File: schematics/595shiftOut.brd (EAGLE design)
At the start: 160 x 100 mm, 7 parts, among them IC1 74HC595N, IC2 74HC595N, U1 TINY45-20-DIP

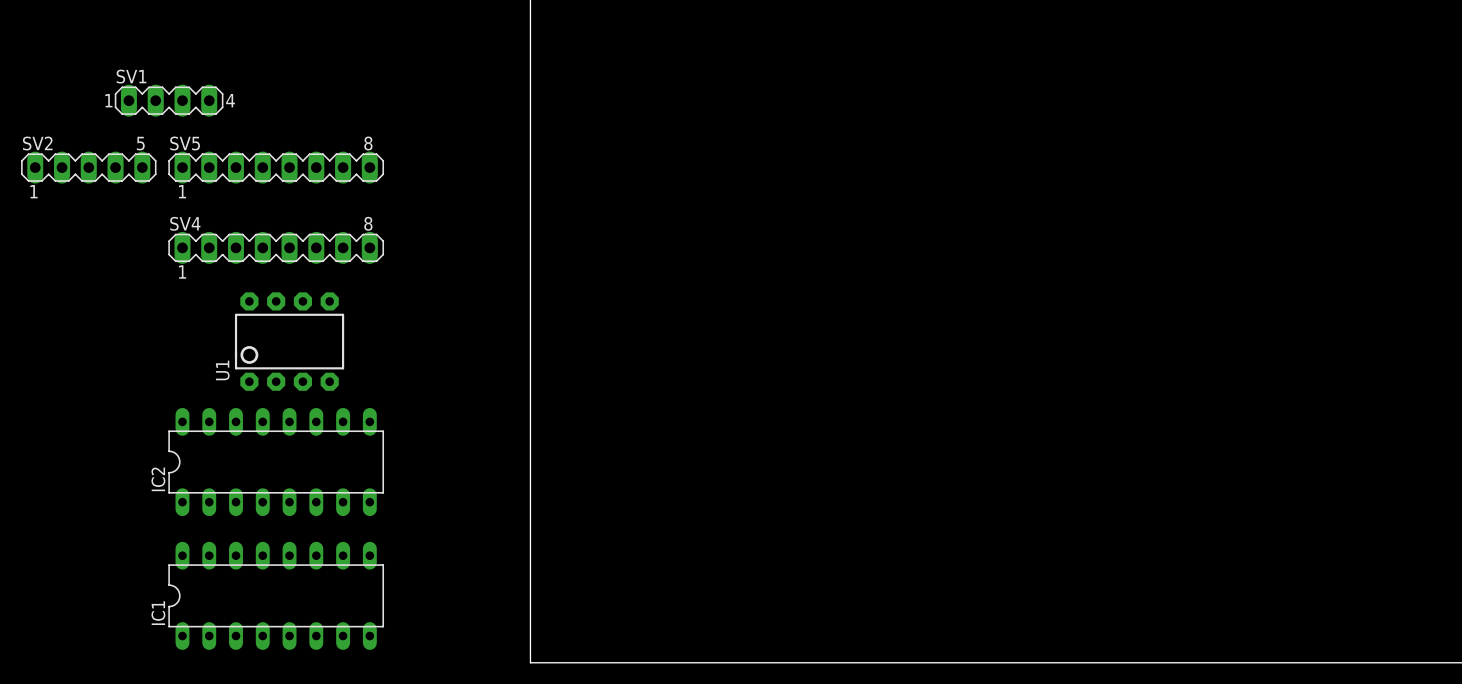
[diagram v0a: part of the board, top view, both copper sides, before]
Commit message: rework the schematics for cnc milling
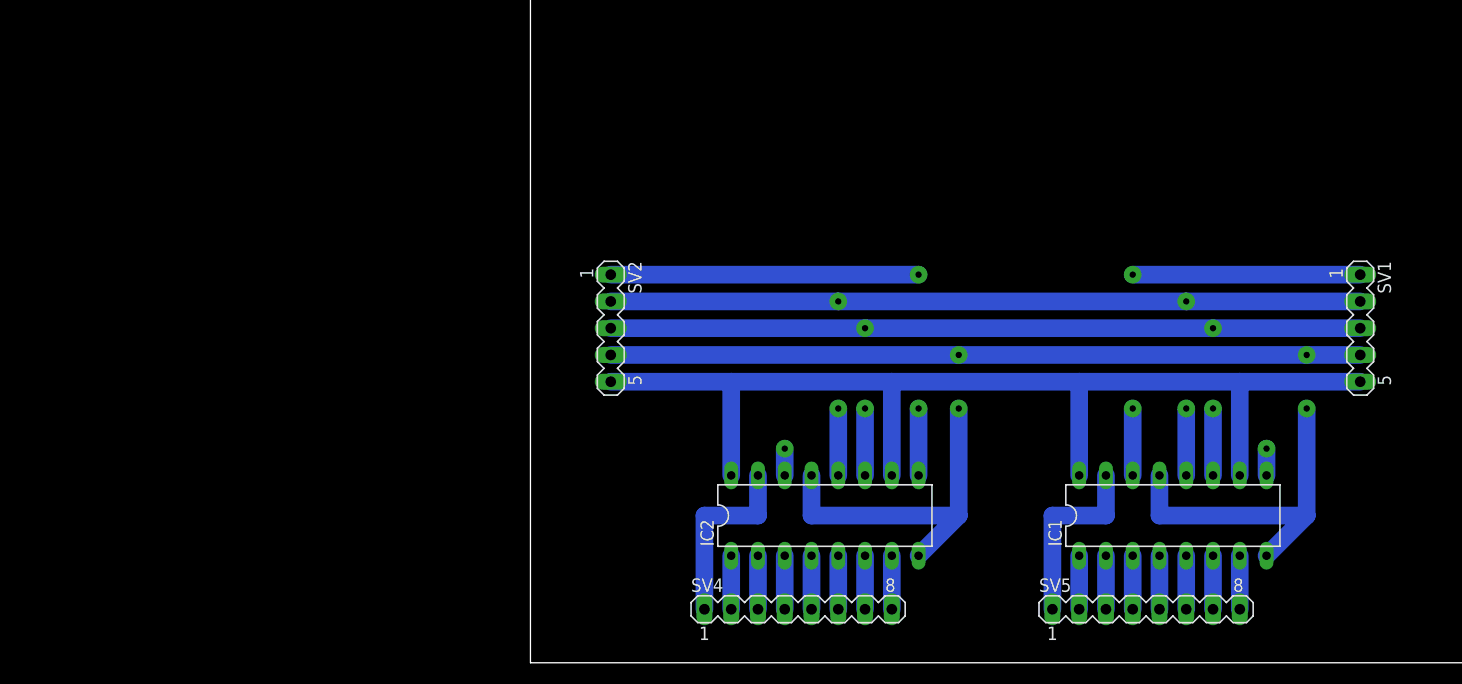
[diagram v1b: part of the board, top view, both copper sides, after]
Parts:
- removed U1: TINY45-20-DIP, SparkFun-DigitalIC:DIP08
- SV1: device con-lstb:MA04-1 -> con-lstb:MA05-1
- moved SV1 115.1 mm to (78.7, 31.8), turned to 270 degrees
- moved SV5 92.6 mm to (58.4, 5.08)
- moved IC1 85.4 mm to (61.0, 14.0)
- moved SV4 60.2 mm to (25.4, 5.08)
- moved IC2 52.3 mm to (27.9, 14.0)
- moved SV2 51.8 mm to (7.62, 31.8), turned to 270 degrees
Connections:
- removed net N$1: SV1.2, U1.5
- removed net N$2: SV1.1, U1.7
- net GND: now also SV1.4; no longer SV1.3, U1.4
- net N$3: now also SV1.1; no longer U1.6
- net N$4: now also SV1.2; no longer U1.2
- net N$5: now also SV1.3; no longer U1.3
- net VCC: now also SV1.5; no longer SV1.4, U1.8
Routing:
- net GND: track 0.00 -> 137.8 mm, vias 0 -> 3
- net VCC: track 0.00 -> 106.7 mm
- net N$5: track 0.00 -> 83.8 mm, vias 0 -> 2
- net N$4: track 0.00 -> 83.8 mm, vias 0 -> 2
- net N$23: track 0.00 -> 35.6 mm, vias 0 -> 1
- net N$3: track 0.00 -> 27.9 mm, vias 0 -> 1
- net N$6: track 0.00 -> 17.8 mm
- net N$14: track 0.00 -> 17.8 mm
- net N$9: track 0.00 -> 5.08 mm
- net N$8: track 0.00 -> 5.08 mm
- net N$7: track 0.00 -> 5.08 mm
- net N$21: track 0.00 -> 5.08 mm
- net N$20: track 0.00 -> 5.08 mm
- net N$19: track 0.00 -> 5.08 mm
- net N$18: track 0.00 -> 5.08 mm
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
